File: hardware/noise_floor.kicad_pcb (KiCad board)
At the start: 2 copper layers, 45.4 x 61.6 mm, 14 parts, among them J1 DC Power, J10 IO/Switch Connector 2 (Switch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, J11 Battery, J2 Input, J3 Output, J6 IO/Effect Connector 1 (IO Sid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, J7 IO/Switch Connector 1 (IO Sid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, J8 IO/Switch Connector 2 (IO Sid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, J9 IO/Switch Connector 1 (Switch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, SW1 Footswitch

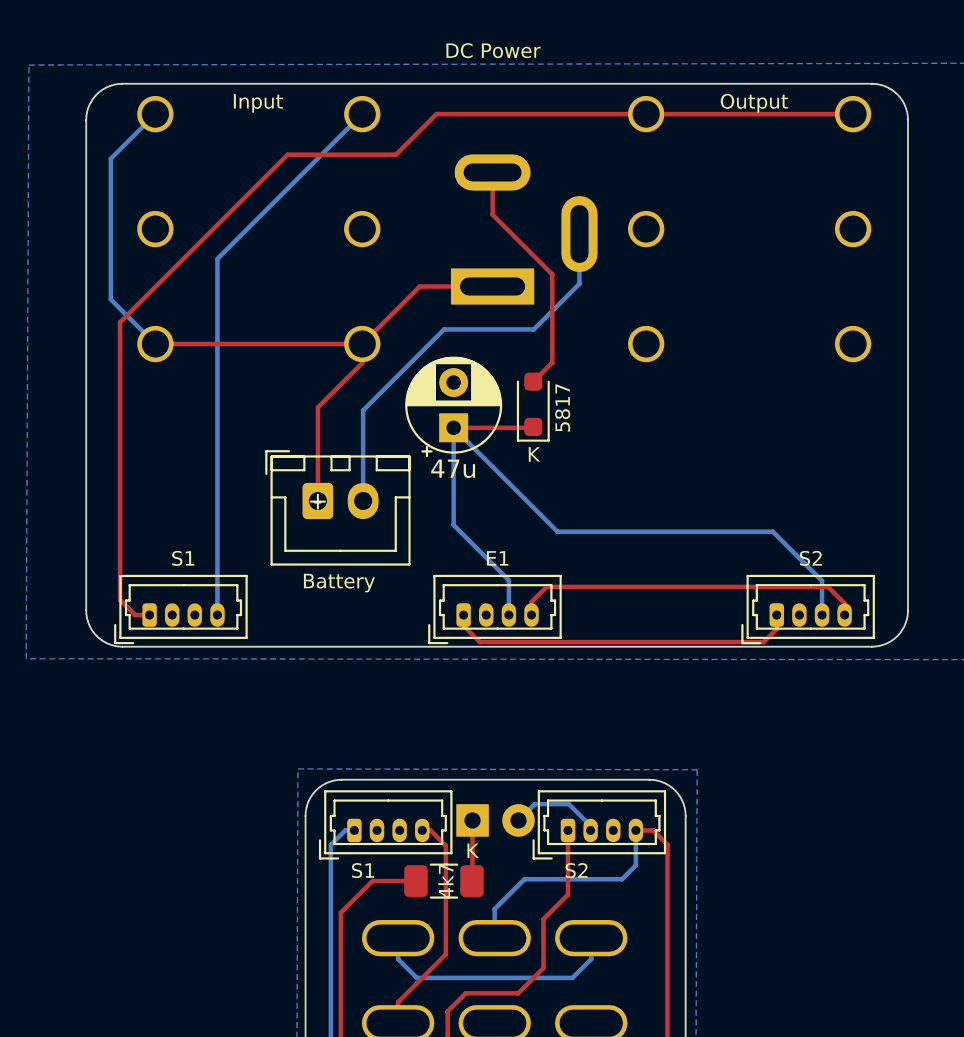
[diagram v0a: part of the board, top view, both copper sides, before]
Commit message: Address issues identified in hardware rev v0.1
 - ACJS-MHOM footprint was pinned backwards. Confirmed operation when flipped to other side of board + rotated backwards.
 - Fix silkscreen: Move DC jack label within board bounds, add battery +/- indicators
 - Slightly shift DC power jack to better align to enclosure bounds.
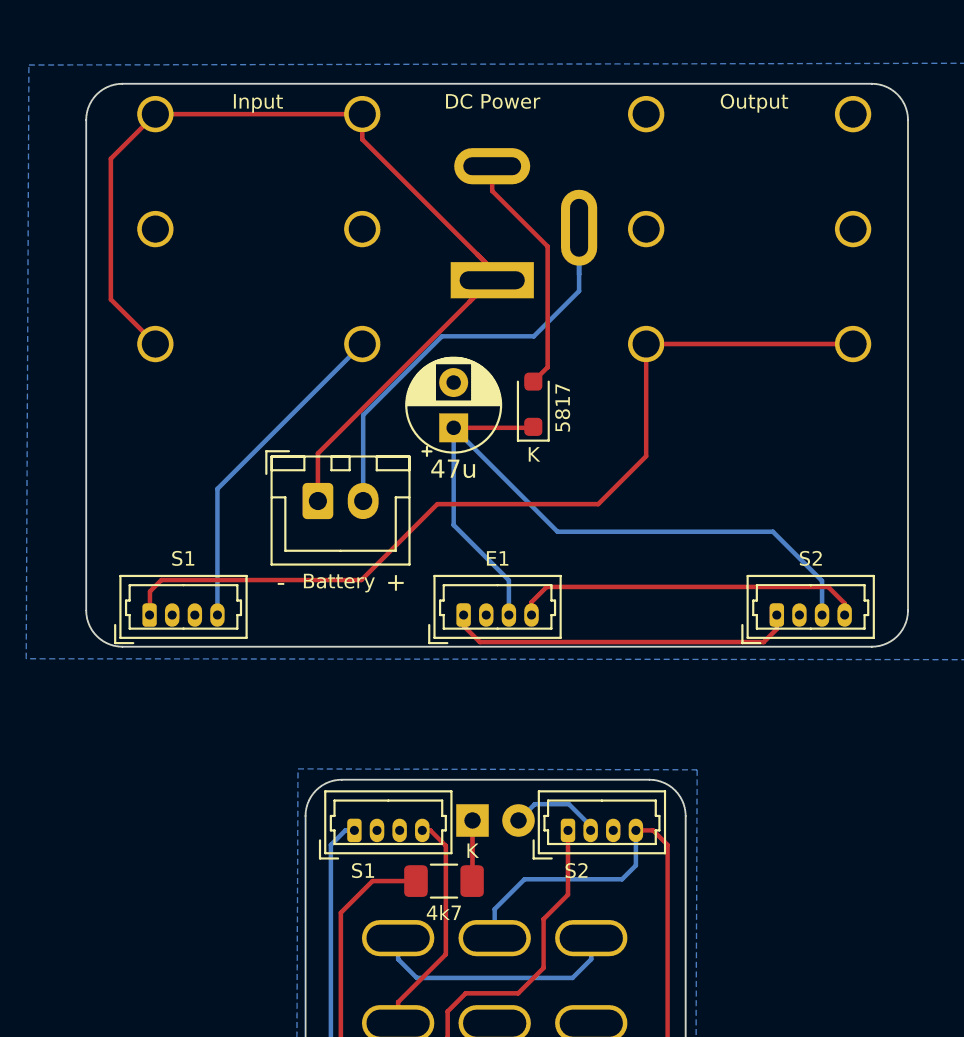
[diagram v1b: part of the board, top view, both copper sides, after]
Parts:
- moved J1 0.35 mm to (40.9, 27.3)
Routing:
- net /BATTERY_NEG: track 44.4 -> 57.7 mm
- net /OUTPUT_TIP_IO: track 62.6 -> 49.4 mm
- net /INPUT_TIP_IO: track 31.0 -> 18.3 mm
- net /BATTERY_POS: track 22.6 -> 25.8 mm
- net /DC_SHIELD: track 13.4 -> 14.3 mm

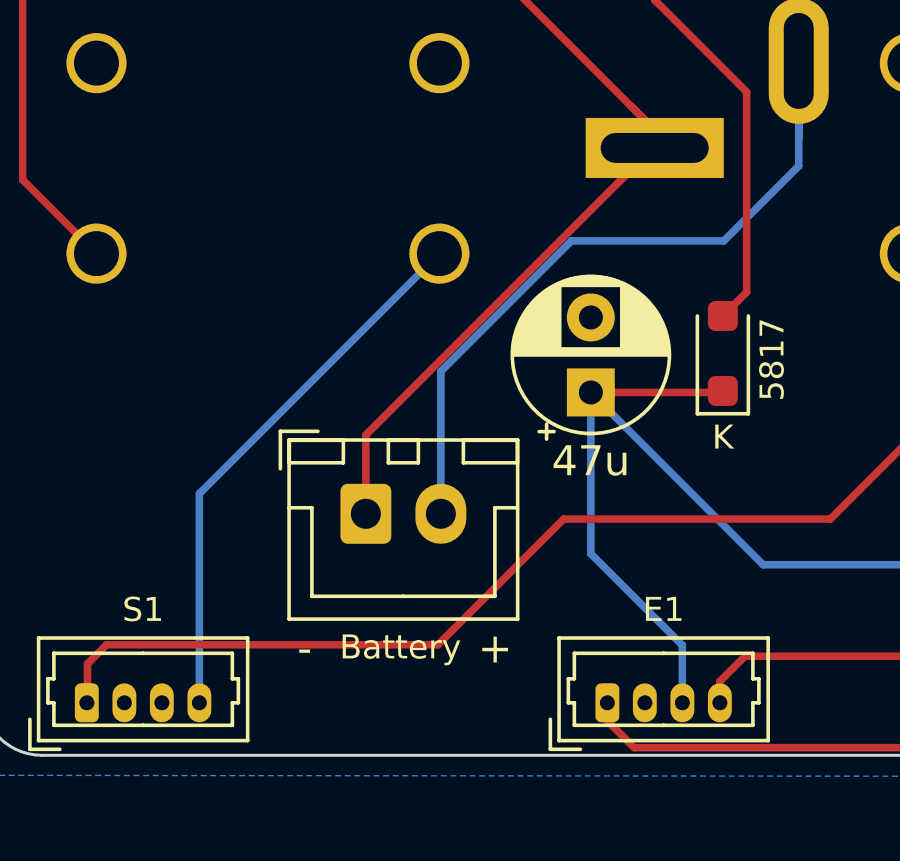
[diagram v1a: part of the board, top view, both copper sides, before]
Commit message: Fix one issue discovered in testing of v0.2 hardware
 - swap nets on battery JST connector
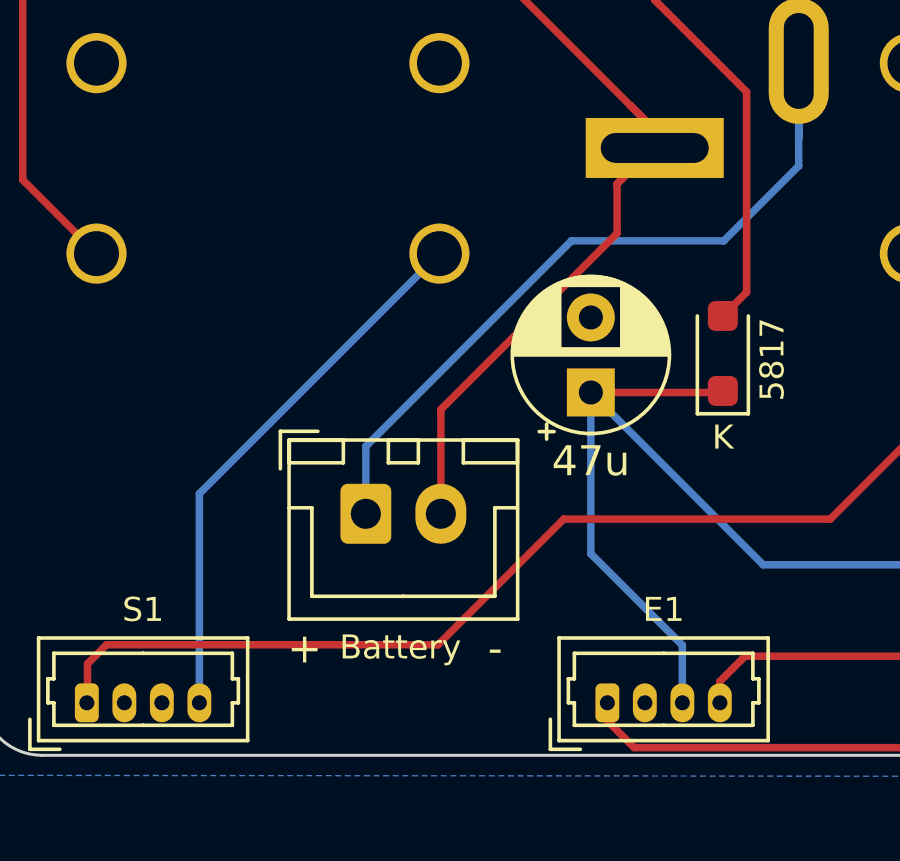
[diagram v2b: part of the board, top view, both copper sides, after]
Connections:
- J11 pad 1: /BATTERY_NEG -> /BATTERY_POS
- J11 pad 2: /BATTERY_POS -> /BATTERY_NEG
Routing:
- net /BATTERY_POS: track 25.8 -> 26.8 mm
- net /BATTERY_NEG: track 57.7 -> 56.6 mm
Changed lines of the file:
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@@
   (title_block
     (title "Noise Floor Interface Boards")
-    (date "2023-03-16")
-    (rev "v0.2")
+    (date "2023-03-23")
+    (rev "v0.21")
     (comment 1 "github.com/whbeers/noise_floor")
   )
@@
         (effects (font (size 0.8 0.8) (thickness 0.15)))
     )
-    (fp_text user "+" (at 4.31 4.492 unlocked) (layer "F.SilkS")
-        (effects (font (size 1 1) (thickness 0.15)))
-    )
-    (fp_text user "-" (at -2.04 4.492 unlocked) (layer "F.SilkS")
+    (fp_text user "+" (at -2.04 4.492 unlocked) (layer "F.SilkS")
+        (effects (font (size 1 1) (thickness 0.15)))
+    )
+    (fp_text user "-" (at 4.31 4.492 unlocked) (layer "F.SilkS")
         (effects (font (size 1 1) (thickness 0.15)))
     )
@@
       (stroke (width 0.1) (type solid)) (layer "F.Fab"))
     (pad "1" thru_hole roundrect (at 0 0) (size 1.7 2) (drill 1) (layers "*.Cu" "*.Mask") (roundrect_rratio 0.147059)
-      (net 14 "/BATTERY_NEG") (pinfunction "Pin_1") (pintype "passive"))
+      (net 16 "/BATTERY_POS") (pinfunction "Pin_1") (pintype "passive"))
     (pad "2" thru_hole oval (at 2.5 0) (size 1.7 2) (drill 1) (layers "*.Cu" "*.Mask")
-      (net 16 "/BATTERY_POS") (pinfunction "Pin_2") (pintype "passive"))
+      (net 14 "/BATTERY_NEG") (pinfunction "Pin_2") (pintype "passive"))
     (model "${KICAD6_3DMODEL_DIR}/Connector_JST.3dshapes/JST_XH_B2B-XH-A_1x02_P2.50mm_Vertical.wrl"
       (offset (xyz 0 0 0))
@@
   (segment (start 35.682 71.832) (end 35.682 72.996) (width 0.25) (layer "F.Cu") (net 13))
   (segment (start 38.416 69.098) (end 35.682 71.832) (width 0.25) (layer "F.Cu") (net 13))
+  (segment (start 39.624 28.448) (end 39.624 30.099) (width 0.25) (layer "F.Cu") (net 14))
   (segment (start 40.879 27.255) (end 40.879 26.655) (width 0.25) (layer "F.Cu") (net 14))
   (segment (start 33.701 19.477) (end 33.701 18.0771) (width 0.25) (layer "F.Cu") (net 14))
   (segment (start 40.005 28.067) (end 39.624 28.448) (width 0.25) (layer "F.Cu") (net 14))
-  (segment (start 39.624 28.448) (end 31.25 36.822) (width 0.25) (layer "F.Cu") (net 14))
-  (segment (start 31.25 36.822) (end 31.25 39.45) (width 0.25) (layer "F.Cu") (net 14))
   (segment (start 40.817 27.255) (end 39.624 28.448) (width 0.25) (layer "F.Cu") (net 14))
   (segment (start 40.879 26.655) (end 40.0685 25.8445) (width 0.25) (layer "F.Cu") (net 14))
   (segment (start 22.271 18.0771) (end 19.812 20.5361) (width 0.25) (layer "F.Cu") (net 14))
+  (segment (start 33.909 35.814) (end 33.75 35.973) (width 0.25) (layer "F.Cu") (net 14))
   (segment (start 40.64 26.416) (end 40.0685 25.8445) (width 0.25) (layer "F.Cu") (net 14))
   (segment (start 19.812 28.3181) (end 22.271 30.7771) (width 0.25) (layer "F.Cu") (net 14))
+  (segment (start 39.624 30.099) (end 33.909 35.814) (width 0.25) (layer "F.Cu") (net 14))
   (segment (start 33.701 18.0771) (end 22.271 18.0771) (width 0.25) (layer "F.Cu") (net 14))
   (segment (start 40.005 27.051) (end 40.005 28.067) (width 0.25) (layer "F.Cu") (net 14))
@@
   (segment (start 40.0685 25.8445) (end 33.701 19.477) (width 0.25) (layer "F.Cu") (net 14))
   (segment (start 40.879 27.255) (end 40.817 27.255) (width 0.25) (layer "F.Cu") (net 14))
+  (segment (start 33.75 35.973) (end 33.75 39.45) (width 0.25) (layer "F.Cu") (net 14))
   (segment (start 19.812 20.5361) (end 19.812 28.3181) (width 0.25) (layer "F.Cu") (net 14))
   (segment (start 39.791 57.098) (end 39.791 60.423) (width 0.25) (layer "F.Cu") (net 15))
   (segment (start 45.679 24.151) (end 45.679 26.924) (width 0.25) (layer "B.Cu") (net 16))
+  (segment (start 45.679 26.924) (end 45.679 24.355) (width 0.25) (layer "B.Cu") (net 16))
+  (segment (start 43.18 30.353) (end 38.1 30.353) (width 0.25) (layer "B.Cu") (net 16))
+  (segment (start 31.25 37.203) (end 31.25 39.45) (width 0.25) (layer "B.Cu") (net 16))
   (segment (start 45.679 26.924) (end 45.679 27.854) (width 0.25) (layer "B.Cu") (net 16))
-  (segment (start 45.679 26.924) (end 45.679 24.355) (width 0.25) (layer "B.Cu") (net 16))
-  (segment (start 38.1 30.353) (end 33.75 34.703) (width 0.25) (layer "B.Cu") (net 16))
+  (segment (start 38.1 30.353) (end 31.25 37.203) (width 0.25) (layer "B.Cu") (net 16))
   (segment (start 45.679 27.854) (end 43.18 30.353) (width 0.25) (layer "B.Cu") (net 16))
-  (segment (start 33.75 34.703) (end 33.75 39.45) (width 0.25) (layer "B.Cu") (net 16))
-  (segment (start 43.18 30.353) (end 38.1 30.353) (width 0.25) (layer "B.Cu") (net 16))
   (segment (start 46.316 57.398) (end 45.116 56.198) (width 0.25) (layer "B.Cu") (net 17))
   (segment (start 43.231 56.198) (end 42.331 57.098) (width 0.25) (layer "B.Cu") (net 17))

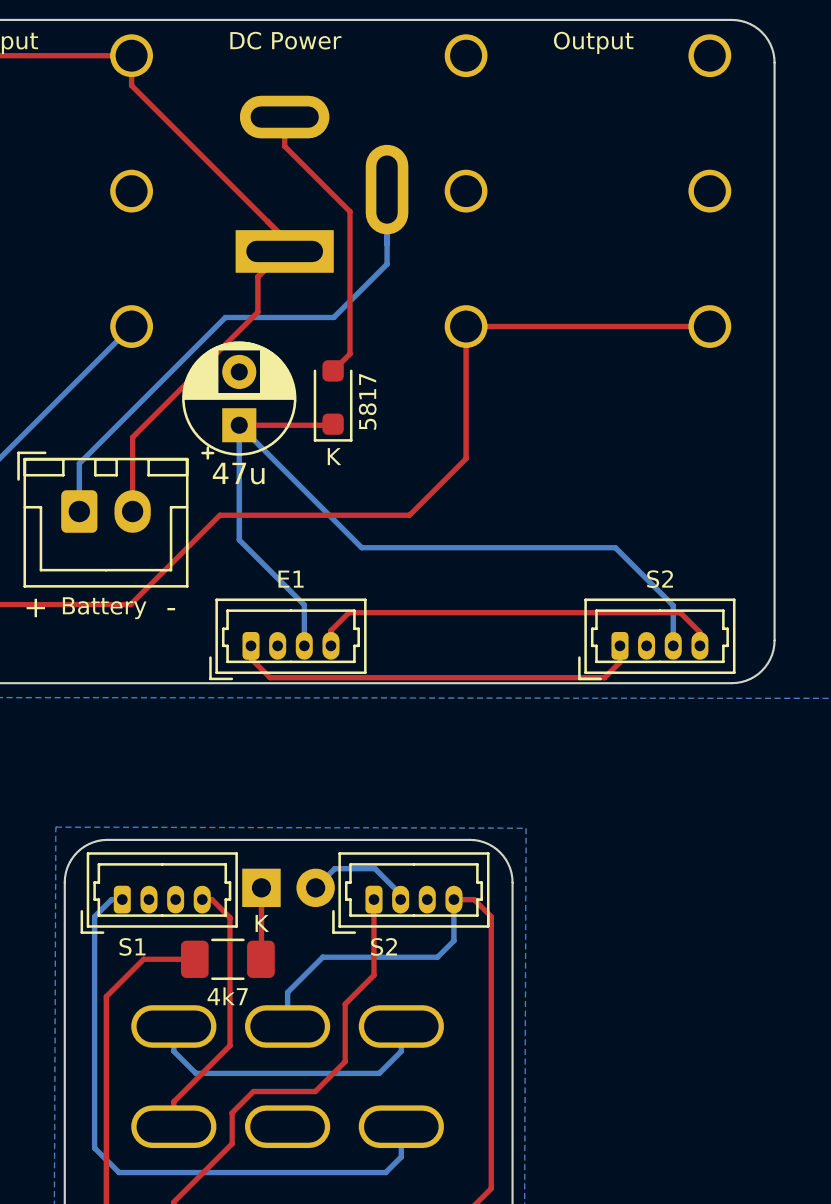
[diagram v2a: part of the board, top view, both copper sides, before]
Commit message: improve power filtering and move to more SMD components
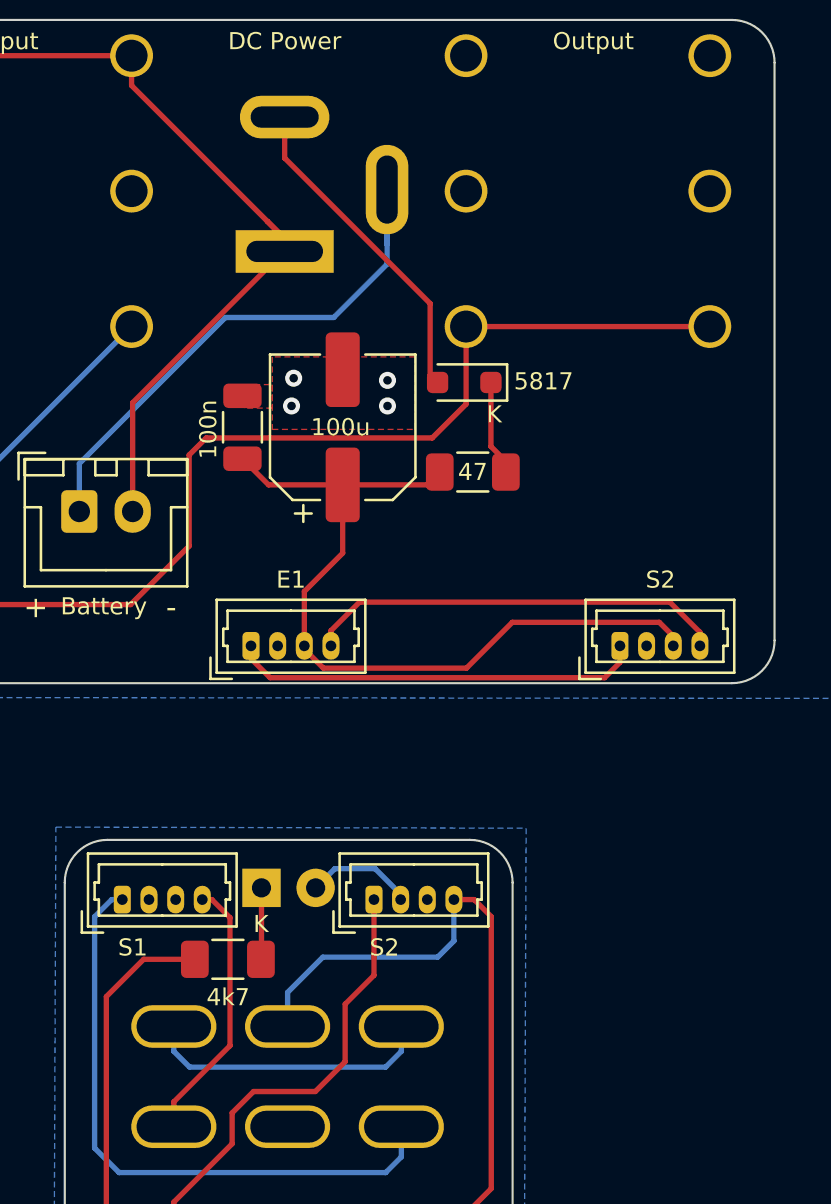
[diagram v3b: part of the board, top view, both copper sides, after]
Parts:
- added C2: 100n, Capacitor_SMD:C_1206_3216Metric, F.Cu at (38.9, 35.5)
- added R2: 47, Resistor_SMD:R_1206_3216Metric_Pad1.30x1.75mm_HandSolder, F.Cu at (49.7, 37.6)
- C1: value 47u -> 100u; footprint Capacitor_THT:CP_Radial_D5.0mm_P2.50mm -> Capacitor_SMD:CP_Elec_6.3x7.7
- moved D2 6.19 mm to (49.3, 33.4), turned to 180 degrees
- moved C1 4.85 mm to (43.6, 35.5)
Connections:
- D2 pad 1: /9V0_IO -> Net-(D2-K)
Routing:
- net /9V0_IO: track 41.7 -> 37.7 mm
- net Net-(D2-K): track 0.00 -> 3.85 mm
- net /DC_SHIELD: track 14.3 -> 16.3 mm
- net /OUTPUT_TIP_IO: track 49.4 -> 50.4 mm
- net GND: vias 0 -> 4
- added copper zone on F.Cu, net GND

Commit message: v0.30 includes a new "ux" board, with the initial feature set:
 - board-to-board connector interface for expandability
 - three potentiometers and three SPDT switches
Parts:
- added J4: UX1, noise_floor:Amphenol_Receptacle_15pin_10162581-3134115LF, F.Cu at (40.9, 99.2)
- added J5: UX2, noise_floor:Amphenol_Receptacle_15pin_10162581-3134115LF, F.Cu at (41.0, 109.8)
- added RV1: POT1, noise_floor:Potentiometer_Single_3_Horizontal, B.Cu at (25.0, 104.2)
- added RV2: POT2, noise_floor:Potentiometer_Single_3_Horizontal, B.Cu at (57.0, 104.2)
- added RV3: POT3, noise_floor:Potentiometer_Single_3_Horizontal, B.Cu at (41.0, 93.8)
- added SW1: SPDT1, noise_floor:SW_SPDT_SOLDER_LUGS, B.Cu at (27.1, 120.8)
- added SW2: SPDT2, noise_floor:SW_SPDT_SOLDER_LUGS, B.Cu at (41.0, 120.8)
- added SW3: SPDT3, noise_floor:SW_SPDT_SOLDER_LUGS, B.Cu at (54.9, 120.8)
- renumbered SW1 to SW4
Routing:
- net /SPDT2_NO: track 0.00 -> 22.2 mm, vias 0 -> 1
- net /POT2_CCW: track 0.00 -> 20.7 mm
- net /POT1_CW: track 0.00 -> 20.5 mm
- net /SPDT3_NO: track 0.00 -> 19.6 mm
- net /SPDT1_NO: track 0.00 -> 19.5 mm
- net /POT1_WIPER: track 0.00 -> 18.0 mm
- net /SPDT2_COM: track 0.00 -> 17.4 mm, vias 0 -> 1
- net /POT2_WIPER: track 0.00 -> 17.0 mm
- net /SPDT3_COM: track 0.00 -> 16.2 mm
- net /SPDT1_COM: track 0.00 -> 16.2 mm
- net /GND_UX: track 0.00 -> 14.1 mm, vias 0 -> 8
- net /POT2_CW: track 0.00 -> 13.2 mm
- net /POT1_CCW: track 0.00 -> 13.0 mm
- net /SPDT1_NC: track 0.00 -> 12.6 mm
- net /SPDT3_NC: track 0.00 -> 12.6 mm
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- added copper zone on B.Cu, net /GND_UX
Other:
- board size 45.4 x 61.6 mm -> 46 x 111.6 mm

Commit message: Add pot adjustment resistors, adapt to different layout and reroute, bump to v0.31
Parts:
- added R1: 0, Resistor_THT:R_Axial_DIN0207_L6.3mm_D2.5mm_P7.62mm_Horizontal, F.Cu at (25.0, 101.9)
- added R10: 0, Resistor_THT:R_Axial_DIN0207_L6.3mm_D2.5mm_P7.62mm_Horizontal, F.Cu at (57.0, 101.9)
- added R2: 0, Resistor_THT:R_Axial_DIN0207_L6.3mm_D2.5mm_P7.62mm_Horizontal, F.Cu at (21.2, 115.2)
- added R3: 0, Resistor_THT:R_Axial_DIN0207_L6.3mm_D2.5mm_P7.62mm_Horizontal, F.Cu at (35.0, 90.5)
- added R5: 0, Resistor_THT:R_Axial_DIN0207_L6.3mm_D2.5mm_P7.62mm_Horizontal, F.Cu at (22.0, 101.9)
- added R6: 0, Resistor_THT:R_Axial_DIN0207_L6.3mm_D2.5mm_P7.62mm_Horizontal, F.Cu at (44.8, 90.5)
- added R7: 0, Resistor_THT:R_Axial_DIN0207_L6.3mm_D2.5mm_P7.62mm_Horizontal, F.Cu at (60.0, 101.9)
- added R8: 0, Resistor_THT:R_Axial_DIN0207_L6.3mm_D2.5mm_P7.62mm_Horizontal, F.Cu at (46.9, 90.5)
- added R9: 0, Resistor_THT:R_Axial_DIN0207_L6.3mm_D2.5mm_P7.62mm_Horizontal, F.Cu at (53.2, 115.2)
- moved J5 15.1 mm to (51.1, 98.5), turned to -90 degrees
- moved J4 10.0 mm to (30.9, 98.5), turned to 90 degrees
- moved RV1 4.21 mm to (25.0, 108.4)
- moved RV3 4.21 mm to (57.0, 108.4)
- moved SW2 4.21 mm to (27.1, 125.0)
- moved SW3 4.21 mm to (41.0, 125.0)
- moved SW4 4.21 mm to (54.9, 125.0)
- moved RV2 3.90 mm to (41.0, 97.7)
- renumbered D2 to D1, D1 to D2, J9 to J10, J10 to J11, J11 to J6, J6 to J7, J7 to J8, J8 to J9, R1 to R11, R2 to R4, RV3 to RV2, RV2 to RV3, SW4 to SW1, SW1 to SW2, SW2 to SW3, SW3 to SW4
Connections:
- J4 pad 1: /POT1_CW -> /SPDT1_NC
- J4 pad 10: unconnected-(J4-Pin_10-Pad10) -> /POT1_WIPER
- J4 pad 11: /POT2_CW -> /POT3_CW
- J4 pad 12: unconnected-(J4-Pin_12-Pad12) -> /POT1_CCW
- J4 pad 13: /POT2_WIPER -> /POT3_WIPER
- J4 pad 14: /POT3_CW -> /POT1_CW
- J4 pad 15: /POT2_CCW -> /POT3_CCW
- J4 pad 2: /POT3_CCW -> /GND_UX
- J4 pad 3: /POT1_WIPER -> /SPDT1_COM
- J4 pad 5: /POT1_CCW -> /SPDT1_NO
- J4 pad 7: /GND_UX -> unconnected-(J4-Pin_7-Pad7)
- J4 pad 8: /POT3_WIPER -> unconnected-(J4-Pin_8-Pad8)
- J4 pad 9: /GND_UX -> unconnected-(J4-Pin_9-Pad9)
- J5 pad 1: /GND_UX -> unconnected-(J5-Pin_1-Pad1)
- J5 pad 10: /SPDT1_NO -> unconnected-(J5-Pin_10-Pad10)
- J5 pad 11: unconnected-(J5-Pin_11-Pad11) -> /SPDT3_NO
- J5 pad 12: /SPDT1_COM -> unconnected-(J5-Pin_12-Pad12)
- J5 pad 13: unconnected-(J5-Pin_13-Pad13) -> /SPDT3_COM
- J5 pad 14: /SPDT1_NC -> /GND_UX
- J5 pad 15: /GND_UX -> /SPDT3_NC
- J5 pad 2: /SPDT3_NC -> /POT2_CCW
- J5 pad 4: /SPDT3_COM -> /POT2_CW
- J5 pad 5: unconnected-(J5-Pin_5-Pad5) -> /SPDT2_NC
- J5 pad 6: /SPDT3_NO -> /POT2_WIPER
- J5 pad 8: /SPDT2_NC -> unconnected-(J5-Pin_8-Pad8)
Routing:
- net /POT3_WIPER: track 7.14 -> 43.2 mm
- net /SPDT2_NC: track 4.10 -> 26.9 mm
- net /SPDT1_NO: track 19.5 -> 34.2 mm
- net /SPDT3_NO: track 19.6 -> 34.2 mm
- net /POT3_CW: track 7.97 -> 21.9 mm
- net /SPDT2_COM: track 17.4 -> 30.6 mm, vias 1 -> 0
- net /SPDT2_NO: track 22.2 -> 34.4 mm, vias 1 -> 0
- net /SPDT1_COM: track 16.2 -> 28.2 mm
- net /SPDT3_COM: track 16.2 -> 28.1 mm
- net /SPDT3_NC: track 12.6 -> 23.6 mm
- net /GND_UX: track 14.1 -> 3.23 mm, vias 8 -> 2
- net /POT1_CCW: track 13.0 -> 23.3 mm
- net /POT2_CW: track 13.2 -> 23.4 mm
- net /SPDT1_NC: track 12.6 -> 21.9 mm
- net /POT2_WIPER: track 17.0 -> 23.5 mm, vias 0 -> 1
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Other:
- board size 46 x 111.6 mm -> 46 x 115.8 mm
